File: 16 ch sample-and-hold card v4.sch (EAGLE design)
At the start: 30 parts, among them IC1 TL074D, IC2 TL074D, IC3 TL074D, IC4 TL074D, IC7 4051D, IC8 4051D

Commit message: Added 5v reg for muxes directly on board
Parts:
- added C1: 0.1uF, resistor:C-EUC0603
- added C3: 0.33uF, resistor:C-EUC0603
- added IC5: 78L05F, linear:78L05F
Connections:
- net +15V: now also C3.2, IC5.VI
- net +5V: now also C1.2, IC5.VO; no longer SV3.5
- net AGND: now also C1.1, C2.1, C3.1, C40.1, IC5.GND, IC5.GND@1, IC7P.GND, IC7P.VEE, IC8P.GND, IC8P.VEE
- net DGND: now also SV3.5; no longer C2.1, C40.1, IC7P.GND, IC7P.VEE, IC8P.GND, IC8P.VEE
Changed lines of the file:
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@@
 <part name="IC8" library="40xx" library_urn="urn:adsk.eagle:library:80" deviceset="4051" device="D" package3d_urn="urn:adsk.eagle:package:821/2"/>
 <part name="SUPPLY1" library="supply2" library_urn="urn:adsk.eagle:library:372" deviceset="+5V" device=""/>
-<part name="SUPPLY2" library="supply2" library_urn="urn:adsk.eagle:library:372" deviceset="DGND" device=""/>
-<part name="SUPPLY3" library="supply2" library_urn="urn:adsk.eagle:library:372" deviceset="DGND" device=""/>
 <part name="SUPPLY4" library="supply2" library_urn="urn:adsk.eagle:library:372" deviceset="+5V" device=""/>
+<part name="IC5" library="linear" library_urn="urn:adsk.eagle:library:262" deviceset="78L*" device="F" package3d_urn="urn:adsk.eagle:package:16478/2" technology="05"/>
+<part name="P+3" library="supply1" deviceset="+15V" device=""/>
+<part name="SUPPLY5" library="supply2" library_urn="urn:adsk.eagle:library:372" deviceset="+5V" device=""/>
+<part name="AGND6" library="supply1" deviceset="AGND" device=""/>
+<part name="AGND7" library="supply1" deviceset="AGND" device=""/>
+<part name="C1" library="resistor" deviceset="C-EU" device="C0603" value="0.1uF"/>
+<part name="C3" library="resistor" deviceset="C-EU" device="C0603" value="0.33uF"/>
+<part name="AGND8" library="supply1" deviceset="AGND" device=""/>
 </parts>
 <sheets>
@@
 <attribute name="VALUE" x="-85.725" y="109.855" size="1.778" layer="96"/>
 </instance>
-<instance part="SUPPLY2" gate="G$1" x="-83.82" y="86.36" smashed="yes">
-<attribute name="VALUE" x="-86.487" y="83.185" size="1.778" layer="96"/>
-</instance>
-<instance part="SUPPLY3" gate="G$1" x="12.7" y="96.52" smashed="yes">
-<attribute name="VALUE" x="10.033" y="93.345" size="1.778" layer="96"/>
-</instance>
 <instance part="SUPPLY4" gate="+5V" x="12.7" y="114.3" smashed="yes">
 <attribute name="VALUE" x="10.795" y="117.475" size="1.778" layer="96"/>
+</instance>
+<instance part="IC5" gate="G$1" x="-91.44" y="63.5" smashed="yes">
+<attribute name="NAME" x="-96.52" y="69.215" size="1.778" layer="95"/>
+<attribute name="VALUE" x="-96.52" y="66.675" size="1.778" layer="96"/>
+</instance>
+<instance part="P+3" gate="1" x="-104.14" y="68.58" smashed="yes">
+<attribute name="VALUE" x="-106.68" y="63.5" size="1.778" layer="96" rot="R90"/>
+</instance>
+<instance part="SUPPLY5" gate="+5V" x="-76.2" y="66.04" smashed="yes">
+<attribute name="VALUE" x="-78.105" y="69.215" size="1.778" layer="96"/>
+</instance>
+<instance part="AGND6" gate="VR1" x="-83.82" y="86.36" smashed="yes">
+<attribute name="VALUE" x="-93.98" y="86.36" size="1.778" layer="96"/>
+</instance>
+<instance part="AGND7" gate="VR1" x="-91.44" y="53.34" smashed="yes">
+<attribute name="VALUE" x="-101.6" y="53.34" size="1.778" layer="96"/>
+</instance>
+<instance part="C1" gate="G$1" x="-76.2" y="58.42" smashed="yes" rot="R180">
+<attribute name="NAME" x="-77.724" y="58.039" size="1.778" layer="95" rot="R180"/>
+<attribute name="VALUE" x="-77.724" y="63.119" size="1.778" layer="96" rot="R180"/>
+</instance>
+<instance part="C3" gate="G$1" x="-104.14" y="58.42" smashed="yes" rot="R180">
+<attribute name="NAME" x="-105.664" y="58.039" size="1.778" layer="95" rot="R180"/>
+<attribute name="VALUE" x="-105.664" y="63.119" size="1.778" layer="96" rot="R180"/>
+</instance>
+<instance part="AGND8" gate="VR1" x="12.7" y="96.52" smashed="yes">
+<attribute name="VALUE" x="2.54" y="96.52" size="1.778" layer="96"/>
 </instance>
 </instances>
@@
 <wire x1="-45.72" y1="-20.32" x2="-55.88" y2="-20.32" width="0.1524" layer="91"/>
 <label x="-55.88" y="-20.32" size="1.778" layer="95"/>
+</segment>
+<segment>
+<pinref part="IC7" gate="P" pin="VEE"/>
+<pinref part="IC7" gate="P" pin="GND"/>
+<wire x1="-88.9" y1="88.9" x2="-83.82" y2="88.9" width="0.1524" layer="91"/>
+<pinref part="IC8" gate="P" pin="VEE"/>
+<pinref part="IC8" gate="P" pin="GND"/>
+<wire x1="-101.6" y1="88.9" x2="-96.52" y2="88.9" width="0.1524" layer="91"/>
+<wire x1="-88.9" y1="88.9" x2="-96.52" y2="88.9" width="0.1524" layer="91"/>
+<junction x="-88.9" y="88.9"/>
+<junction x="-96.52" y="88.9"/>
+<pinref part="AGND6" gate="VR1" pin="AGND"/>
+<junction x="-83.82" y="88.9"/>
+</segment>
+<segment>
+<pinref part="IC5" gate="G$1" pin="GND"/>
+<pinref part="AGND7" gate="VR1" pin="AGND"/>
+<pinref part="C3" gate="G$1" pin="1"/>
+<wire x1="-104.14" y1="55.88" x2="-91.44" y2="55.88" width="0.1524" layer="91"/>
+<junction x="-91.44" y="55.88"/>
+<pinref part="C1" gate="G$1" pin="1"/>
+<wire x1="-76.2" y1="55.88" x2="-88.9" y2="55.88" width="0.1524" layer="91"/>
+<pinref part="IC5" gate="G$1" pin="GND@1"/>
+<wire x1="-88.9" y1="55.88" x2="-91.44" y2="55.88" width="0.1524" layer="91"/>
+<junction x="-88.9" y="55.88"/>
+</segment>
+<segment>
+<pinref part="C2" gate="G$1" pin="1"/>
+<wire x1="25.4" y1="101.6" x2="25.4" y2="99.06" width="0.1524" layer="91"/>
+<wire x1="25.4" y1="99.06" x2="12.7" y2="99.06" width="0.1524" layer="91"/>
+<pinref part="C40" gate="G$1" pin="1"/>
+<wire x1="12.7" y1="99.06" x2="12.7" y2="101.6" width="0.1524" layer="91"/>
+<pinref part="AGND8" gate="VR1" pin="AGND"/>
+<junction x="12.7" y="99.06"/>
 </segment>
 </net>
@@
 <wire x1="-45.72" y1="-38.1" x2="-55.88" y2="-38.1" width="0.1524" layer="91"/>
 <label x="-55.88" y="-38.1" size="1.778" layer="95"/>
+</segment>
+<segment>
+<pinref part="P+3" gate="1" pin="+15V"/>
+<wire x1="-104.14" y1="66.04" x2="-104.14" y2="63.5" width="0.1524" layer="91"/>
+<pinref part="IC5" gate="G$1" pin="VI"/>
+<wire x1="-104.14" y1="63.5" x2="-99.06" y2="63.5" width="0.1524" layer="91"/>
+<pinref part="C3" gate="G$1" pin="2"/>
+<junction x="-104.14" y="63.5"/>
 </segment>
 </net>
@@
 </segment>
 <segment>
-<pinref part="IC7" gate="P" pin="VEE"/>
-<pinref part="IC7" gate="P" pin="GND"/>
-<wire x1="-88.9" y1="88.9" x2="-83.82" y2="88.9" width="0.1524" layer="91"/>
-<pinref part="SUPPLY2" gate="G$1" pin="DGND"/>
-<junction x="-83.82" y="88.9"/>
-<pinref part="IC8" gate="P" pin="VEE"/>
-<pinref part="IC8" gate="P" pin="GND"/>
-<wire x1="-101.6" y1="88.9" x2="-96.52" y2="88.9" width="0.1524" layer="91"/>
-<wire x1="-88.9" y1="88.9" x2="-96.52" y2="88.9" width="0.1524" layer="91"/>
-<junction x="-88.9" y="88.9"/>
-<junction x="-96.52" y="88.9"/>
-</segment>
-<segment>
-<pinref part="C2" gate="G$1" pin="1"/>
-<wire x1="25.4" y1="101.6" x2="25.4" y2="99.06" width="0.1524" layer="91"/>
-<pinref part="SUPPLY3" gate="G$1" pin="DGND"/>
-<wire x1="25.4" y1="99.06" x2="12.7" y2="99.06" width="0.1524" layer="91"/>
-<pinref part="C40" gate="G$1" pin="1"/>
-<wire x1="12.7" y1="99.06" x2="12.7" y2="101.6" width="0.1524" layer="91"/>
-<junction x="12.7" y="99.06"/>
+<pinref part="SV3" gate="G$1" pin="5"/>
+<wire x1="-30.48" y1="-33.02" x2="-20.32" y2="-33.02" width="0.1524" layer="91"/>
+<label x="-30.48" y="-33.02" size="1.778" layer="95"/>
 </segment>
 </net>
@@
 </segment>
 <segment>
-<pinref part="SV3" gate="G$1" pin="5"/>
-<wire x1="-30.48" y1="-33.02" x2="-20.32" y2="-33.02" width="0.1524" layer="91"/>
-<label x="-30.48" y="-33.02" size="1.778" layer="95"/>
-</segment>
-</net>
+<pinref part="IC5" gate="G$1" pin="VO"/>
+<pinref part="SUPPLY5" gate="+5V" pin="+5V"/>
+<wire x1="-81.28" y1="63.5" x2="-76.2" y2="63.5" width="0.1524" layer="91"/>
+<pinref part="C1" gate="G$1" pin="2"/>
+<junction x="-76.2" y="63.5"/>
+</segment>
+</net>

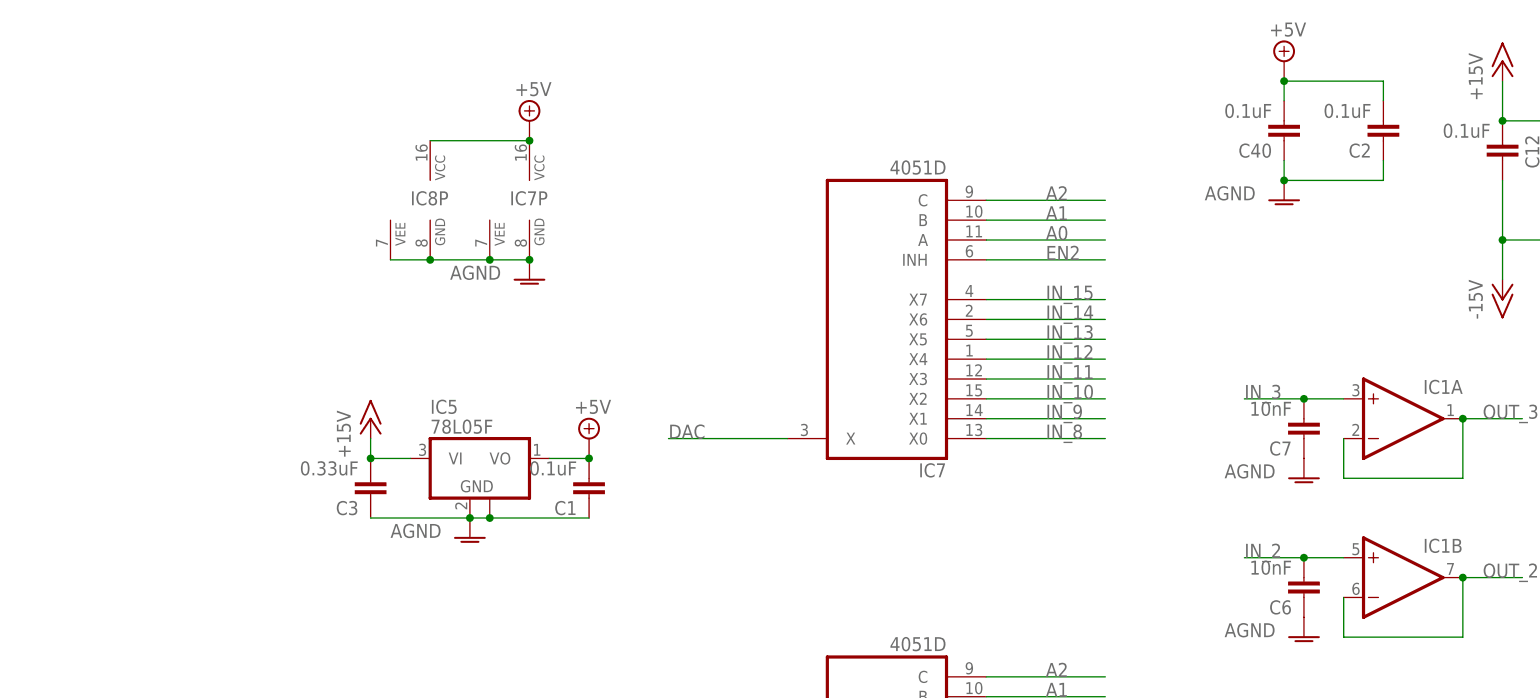
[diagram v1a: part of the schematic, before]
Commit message: Added selectable agnd/dgnd
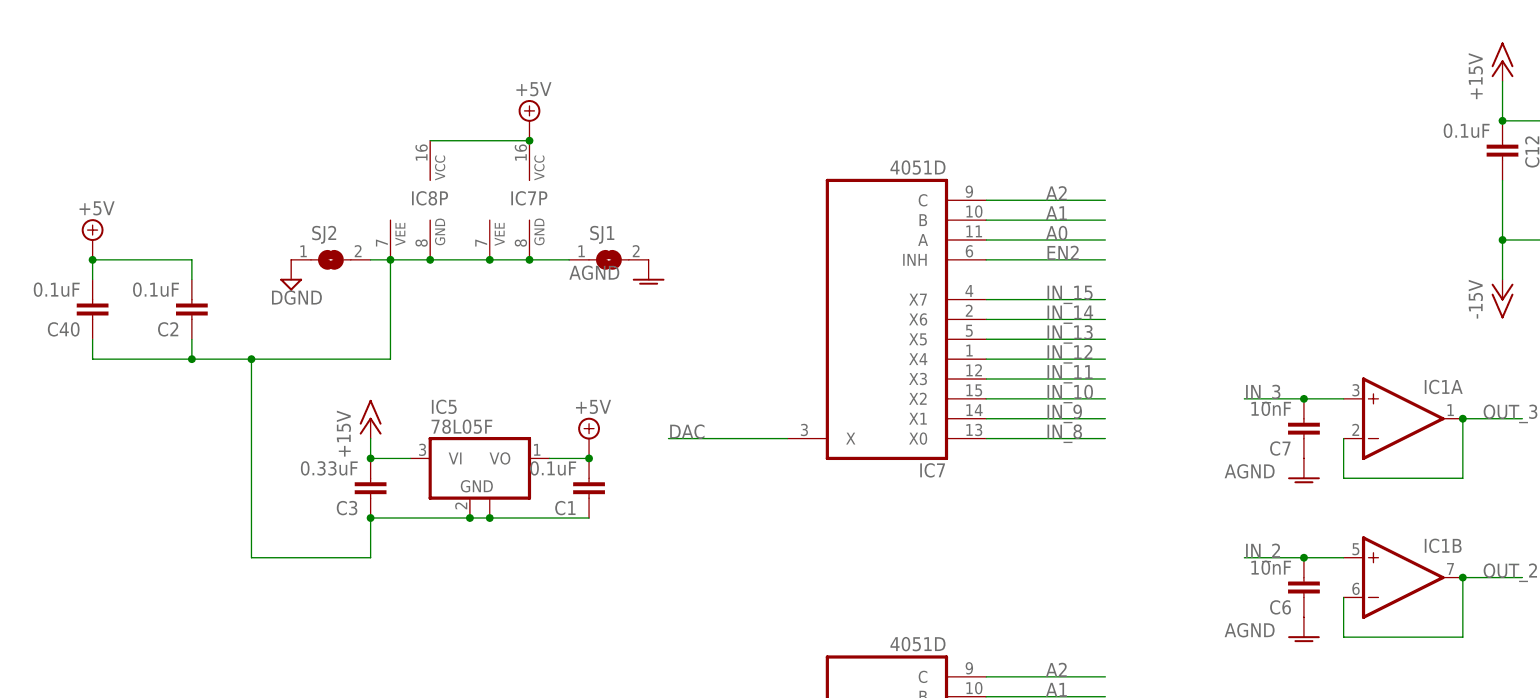
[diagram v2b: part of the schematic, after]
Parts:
- added SJ1, SJ2: (no value), jumper:SJ
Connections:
- new net N$2: C1.1, C2.1, C3.1, C40.1, IC5.GND, IC5.GND@1, IC7P.GND, IC7P.VEE, IC8P.GND, IC8P.VEE, SJ1.1, SJ2.2
- net AGND: now also SJ1.2; no longer C1.1, C2.1, C3.1, C40.1, IC5.GND, IC5.GND@1, IC7P.GND, IC7P.VEE, IC8P.GND, IC8P.VEE
- net DGND: now also SJ2.1
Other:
- moved on the sheet: C2, C40
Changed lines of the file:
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@@
 <part name="P+3" library="supply1" deviceset="+15V" device=""/>
 <part name="SUPPLY5" library="supply2" library_urn="urn:adsk.eagle:library:372" deviceset="+5V" device=""/>
-<part name="AGND6" library="supply1" deviceset="AGND" device=""/>
-<part name="AGND7" library="supply1" deviceset="AGND" device=""/>
 <part name="C1" library="resistor" deviceset="C-EU" device="C0603" value="0.1uF"/>
 <part name="C3" library="resistor" deviceset="C-EU" device="C0603" value="0.33uF"/>
-<part name="AGND8" library="supply1" deviceset="AGND" device=""/>
+<part name="SJ1" library="jumper" library_urn="urn:adsk.eagle:library:252" deviceset="SJ" device="" package3d_urn="urn:adsk.eagle:package:15471/1"/>
+<part name="AGND6" library="supply1" deviceset="AGND" device=""/>
+<part name="SJ2" library="jumper" library_urn="urn:adsk.eagle:library:252" deviceset="SJ" device="" package3d_urn="urn:adsk.eagle:package:15471/1"/>
+<part name="SUPPLY2" library="supply2" library_urn="urn:adsk.eagle:library:372" deviceset="DGND" device=""/>
 </parts>
 <sheets>
@@
 </instance>
 <instance part="AGND5" gate="VR1" x="-55.88" y="-88.9" smashed="yes"/>
-<instance part="C40" gate="G$1" x="12.7" y="104.14" smashed="yes" rot="R180">
-<attribute name="NAME" x="11.176" y="103.759" size="1.778" layer="95" rot="R180"/>
-<attribute name="VALUE" x="11.176" y="108.839" size="1.778" layer="96" rot="R180"/>
+<instance part="C40" gate="G$1" x="-139.7" y="81.28" smashed="yes" rot="R180">
+<attribute name="NAME" x="-141.224" y="80.899" size="1.778" layer="95" rot="R180"/>
+<attribute name="VALUE" x="-141.224" y="85.979" size="1.778" layer="96" rot="R180"/>
 </instance>
 <instance part="P+2" gate="1" x="-60.96" y="-88.9" smashed="yes">
@@
 <attribute name="VALUE" x="-58.42" y="-101.6" size="1.778" layer="96" rot="R180"/>
 </instance>
-<instance part="C2" gate="G$1" x="25.4" y="104.14" smashed="yes" rot="R180">
-<attribute name="NAME" x="23.876" y="103.759" size="1.778" layer="95" rot="R180"/>
-<attribute name="VALUE" x="23.876" y="108.839" size="1.778" layer="96" rot="R180"/>
+<instance part="C2" gate="G$1" x="-127" y="81.28" smashed="yes" rot="R180">
+<attribute name="NAME" x="-128.524" y="80.899" size="1.778" layer="95" rot="R180"/>
+<attribute name="VALUE" x="-128.524" y="85.979" size="1.778" layer="96" rot="R180"/>
 </instance>
 <instance part="SV3" gate="G$1" x="-38.1" y="-30.48" smashed="yes">
@@
 <attribute name="VALUE" x="-85.725" y="109.855" size="1.778" layer="96"/>
 </instance>
-<instance part="SUPPLY4" gate="+5V" x="12.7" y="114.3" smashed="yes">
-<attribute name="VALUE" x="10.795" y="117.475" size="1.778" layer="96"/>
+<instance part="SUPPLY4" gate="+5V" x="-139.7" y="91.44" smashed="yes">
+<attribute name="VALUE" x="-141.605" y="94.615" size="1.778" layer="96"/>
 </instance>
 <instance part="IC5" gate="G$1" x="-91.44" y="63.5" smashed="yes">
@@
 <attribute name="VALUE" x="-78.105" y="69.215" size="1.778" layer="96"/>
 </instance>
-<instance part="AGND6" gate="VR1" x="-83.82" y="86.36" smashed="yes">
-<attribute name="VALUE" x="-93.98" y="86.36" size="1.778" layer="96"/>
-</instance>
-<instance part="AGND7" gate="VR1" x="-91.44" y="53.34" smashed="yes">
-<attribute name="VALUE" x="-101.6" y="53.34" size="1.778" layer="96"/>
-</instance>
 <instance part="C1" gate="G$1" x="-76.2" y="58.42" smashed="yes" rot="R180">
 <attribute name="NAME" x="-77.724" y="58.039" size="1.778" layer="95" rot="R180"/>
@@
 <attribute name="VALUE" x="-105.664" y="63.119" size="1.778" layer="96" rot="R180"/>
 </instance>
-<instance part="AGND8" gate="VR1" x="12.7" y="96.52" smashed="yes">
-<attribute name="VALUE" x="2.54" y="96.52" size="1.778" layer="96"/>
+<instance part="SJ1" gate="1" x="-73.66" y="88.9" smashed="yes">
+<attribute name="NAME" x="-76.2" y="91.44" size="1.778" layer="95"/>
+<attribute name="VALUE" x="-76.2" y="85.09" size="1.778" layer="96"/>
+</instance>
+<instance part="AGND6" gate="VR1" x="-68.58" y="86.36" smashed="yes">
+<attribute name="VALUE" x="-78.74" y="86.36" size="1.778" layer="96"/>
+</instance>
+<instance part="SJ2" gate="1" x="-109.22" y="88.9" smashed="yes">
+<attribute name="NAME" x="-111.76" y="91.44" size="1.778" layer="95"/>
+<attribute name="VALUE" x="-111.76" y="85.09" size="1.778" layer="96"/>
+</instance>
+<instance part="SUPPLY2" gate="G$1" x="-114.3" y="86.36" smashed="yes">
+<attribute name="VALUE" x="-116.967" y="83.185" size="1.778" layer="96"/>
 </instance>
 </instances>
@@
 </segment>
 <segment>
-<pinref part="IC7" gate="P" pin="VEE"/>
-<pinref part="IC7" gate="P" pin="GND"/>
-<wire x1="-88.9" y1="88.9" x2="-83.82" y2="88.9" width="0.1524" layer="91"/>
-<pinref part="IC8" gate="P" pin="VEE"/>
-<pinref part="IC8" gate="P" pin="GND"/>
-<wire x1="-101.6" y1="88.9" x2="-96.52" y2="88.9" width="0.1524" layer="91"/>
-<wire x1="-88.9" y1="88.9" x2="-96.52" y2="88.9" width="0.1524" layer="91"/>
-<junction x="-88.9" y="88.9"/>
-<junction x="-96.52" y="88.9"/>
+<pinref part="SJ1" gate="1" pin="2"/>
 <pinref part="AGND6" gate="VR1" pin="AGND"/>
-<junction x="-83.82" y="88.9"/>
-</segment>
-<segment>
-<pinref part="IC5" gate="G$1" pin="GND"/>
-<pinref part="AGND7" gate="VR1" pin="AGND"/>
-<pinref part="C3" gate="G$1" pin="1"/>
-<wire x1="-104.14" y1="55.88" x2="-91.44" y2="55.88" width="0.1524" layer="91"/>
-<junction x="-91.44" y="55.88"/>
-<pinref part="C1" gate="G$1" pin="1"/>
-<wire x1="-76.2" y1="55.88" x2="-88.9" y2="55.88" width="0.1524" layer="91"/>
-<pinref part="IC5" gate="G$1" pin="GND@1"/>
-<wire x1="-88.9" y1="55.88" x2="-91.44" y2="55.88" width="0.1524" layer="91"/>
-<junction x="-88.9" y="55.88"/>
-</segment>
-<segment>
-<pinref part="C2" gate="G$1" pin="1"/>
-<wire x1="25.4" y1="101.6" x2="25.4" y2="99.06" width="0.1524" layer="91"/>
-<wire x1="25.4" y1="99.06" x2="12.7" y2="99.06" width="0.1524" layer="91"/>
-<pinref part="C40" gate="G$1" pin="1"/>
-<wire x1="12.7" y1="99.06" x2="12.7" y2="101.6" width="0.1524" layer="91"/>
-<pinref part="AGND8" gate="VR1" pin="AGND"/>
-<junction x="12.7" y="99.06"/>
 </segment>
 </net>
@@
 <label x="-30.48" y="-33.02" size="1.778" layer="95"/>
 </segment>
+<segment>
+<pinref part="SJ2" gate="1" pin="1"/>
+<pinref part="SUPPLY2" gate="G$1" pin="DGND"/>
+</segment>
 </net>
 <net name="OUT_15" class="0">
@@
 <segment>
 <pinref part="SUPPLY4" gate="+5V" pin="+5V"/>
-<wire x1="12.7" y1="111.76" x2="25.4" y2="111.76" width="0.1524" layer="91"/>
+<wire x1="-139.7" y1="88.9" x2="-127" y2="88.9" width="0.1524" layer="91"/>
 <pinref part="C2" gate="G$1" pin="2"/>
-<wire x1="25.4" y1="111.76" x2="25.4" y2="109.22" width="0.1524" layer="91"/>
+<wire x1="-127" y1="88.9" x2="-127" y2="86.36" width="0.1524" layer="91"/>
 <pinref part="C40" gate="G$1" pin="2"/>
-<wire x1="12.7" y1="111.76" x2="12.7" y2="109.22" width="0.1524" layer="91"/>
-<junction x="12.7" y="111.76"/>
+<wire x1="-139.7" y1="88.9" x2="-139.7" y2="86.36" width="0.1524" layer="91"/>
+<junction x="-139.7" y="88.9"/>
 </segment>
 <segment>
@@
 </segment>
 </net>
+<net name="N$2" class="0">
+<segment>
+<pinref part="C2" gate="G$1" pin="1"/>
+<wire x1="-127" y1="78.74" x2="-127" y2="76.2" width="0.1524" layer="91"/>
+<wire x1="-127" y1="76.2" x2="-139.7" y2="76.2" width="0.1524" layer="91"/>
+<pinref part="C40" gate="G$1" pin="1"/>
+<wire x1="-139.7" y1="76.2" x2="-139.7" y2="78.74" width="0.1524" layer="91"/>
+<pinref part="IC7" gate="P" pin="VEE"/>
+<pinref part="IC7" gate="P" pin="GND"/>
+<wire x1="-88.9" y1="88.9" x2="-83.82" y2="88.9" width="0.1524" layer="91"/>
+<pinref part="IC8" gate="P" pin="VEE"/>
+<pinref part="IC8" gate="P" pin="GND"/>
+<wire x1="-101.6" y1="88.9" x2="-96.52" y2="88.9" width="0.1524" layer="91"/>
+<wire x1="-88.9" y1="88.9" x2="-96.52" y2="88.9" width="0.1524" layer="91"/>
+<junction x="-88.9" y="88.9"/>
+<junction x="-96.52" y="88.9"/>
+<pinref part="SJ2" gate="1" pin="2"/>
+<wire x1="-104.14" y1="88.9" x2="-101.6" y2="88.9" width="0.1524" layer="91"/>
+<junction x="-101.6" y="88.9"/>
+<pinref part="SJ1" gate="1" pin="1"/>
+<wire x1="-83.82" y1="88.9" x2="-78.74" y2="88.9" width="0.1524" layer="91"/>
+<junction x="-83.82" y="88.9"/>
+<wire x1="-101.6" y1="88.9" x2="-101.6" y2="76.2" width="0.1524" layer="91"/>
+<wire x1="-101.6" y1="76.2" x2="-119.38" y2="76.2" width="0.1524" layer="91"/>
+<wire x1="-119.38" y1="76.2" x2="-119.38" y2="50.8" width="0.1524" layer="91"/>
+<wire x1="-119.38" y1="50.8" x2="-104.14" y2="50.8" width="0.1524" layer="91"/>
+<pinref part="IC5" gate="G$1" pin="GND"/>
+<pinref part="C3" gate="G$1" pin="1"/>
+<wire x1="-104.14" y1="55.88" x2="-91.44" y2="55.88" width="0.1524" layer="91"/>
+<junction x="-91.44" y="55.88"/>
+<pinref part="C1" gate="G$1" pin="1"/>
+<wire x1="-76.2" y1="55.88" x2="-88.9" y2="55.88" width="0.1524" layer="91"/>
+<pinref part="IC5" gate="G$1" pin="GND@1"/>
+<wire x1="-88.9" y1="55.88" x2="-91.44" y2="55.88" width="0.1524" layer="91"/>
+<junction x="-88.9" y="55.88"/>
+<wire x1="-104.14" y1="50.8" x2="-104.14" y2="55.88" width="0.1524" layer="91"/>
+<junction x="-104.14" y="55.88"/>
+<wire x1="-127" y1="76.2" x2="-119.38" y2="76.2" width="0.1524" layer="91"/>
+<junction x="-127" y="76.2"/>
+<junction x="-119.38" y="76.2"/>
+</segment>
+</net>

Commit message: Added two wires for separate DAC channels to each mux on the SH board
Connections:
- removed net DAC: IC7A.X, IC8A.X, SV3.15
- new net DAC1: IC8A.X, SV3.13
- new net DAC2: IC7A.X, SV3.15
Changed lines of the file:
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@@
 </segment>
 </net>
-<net name="DAC" class="0">
-<segment>
-<wire x1="-50.8" y1="5.08" x2="-60.96" y2="5.08" width="0.1524" layer="91"/>
-<label x="-60.96" y="5.08" size="1.778" layer="95"/>
-<pinref part="IC8" gate="A" pin="X"/>
-</segment>
+<net name="DAC2" class="0">
 <segment>
 <wire x1="-50.8" y1="66.04" x2="-66.04" y2="66.04" width="0.1524" layer="91"/>
@@
 </segment>
 </net>
+<net name="DAC1" class="0">
+<segment>
+<pinref part="SV3" gate="G$1" pin="13"/>
+<wire x1="-30.48" y1="-22.86" x2="-20.32" y2="-22.86" width="0.1524" layer="91"/>
+<label x="-30.48" y="-22.86" size="1.778" layer="95"/>
+</segment>
+<segment>
+<wire x1="-50.8" y1="5.08" x2="-60.96" y2="5.08" width="0.1524" layer="91"/>
+<label x="-60.96" y="5.08" size="1.778" layer="95"/>
+<pinref part="IC8" gate="A" pin="X"/>
+</segment>
+</net>
